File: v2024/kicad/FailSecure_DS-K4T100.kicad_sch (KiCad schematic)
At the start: 82 parts, among them CN1 WJ2EDGRC-5.08-2P, CN2 WJ2EDGRC-5.08-2P, CN3 WJ2EDGRC-5.08-8P, CN4 WAFER-200W-4P, CN5 WJ2EDGRC-5.08-2P, Q1 BSS138, Q3 BSS138, Q4 BSS138, SW1 1TS002B-2300-4301, SW2 1TS002B-2300-4301, U1 PicoW, U2 TPS563200DDCR, U3 BX-DS2.54-4PTP, U4 SFH6206-3T, U5 HX PM2.54-2X5P WT, U6 HX PM2.54-2X5P WT

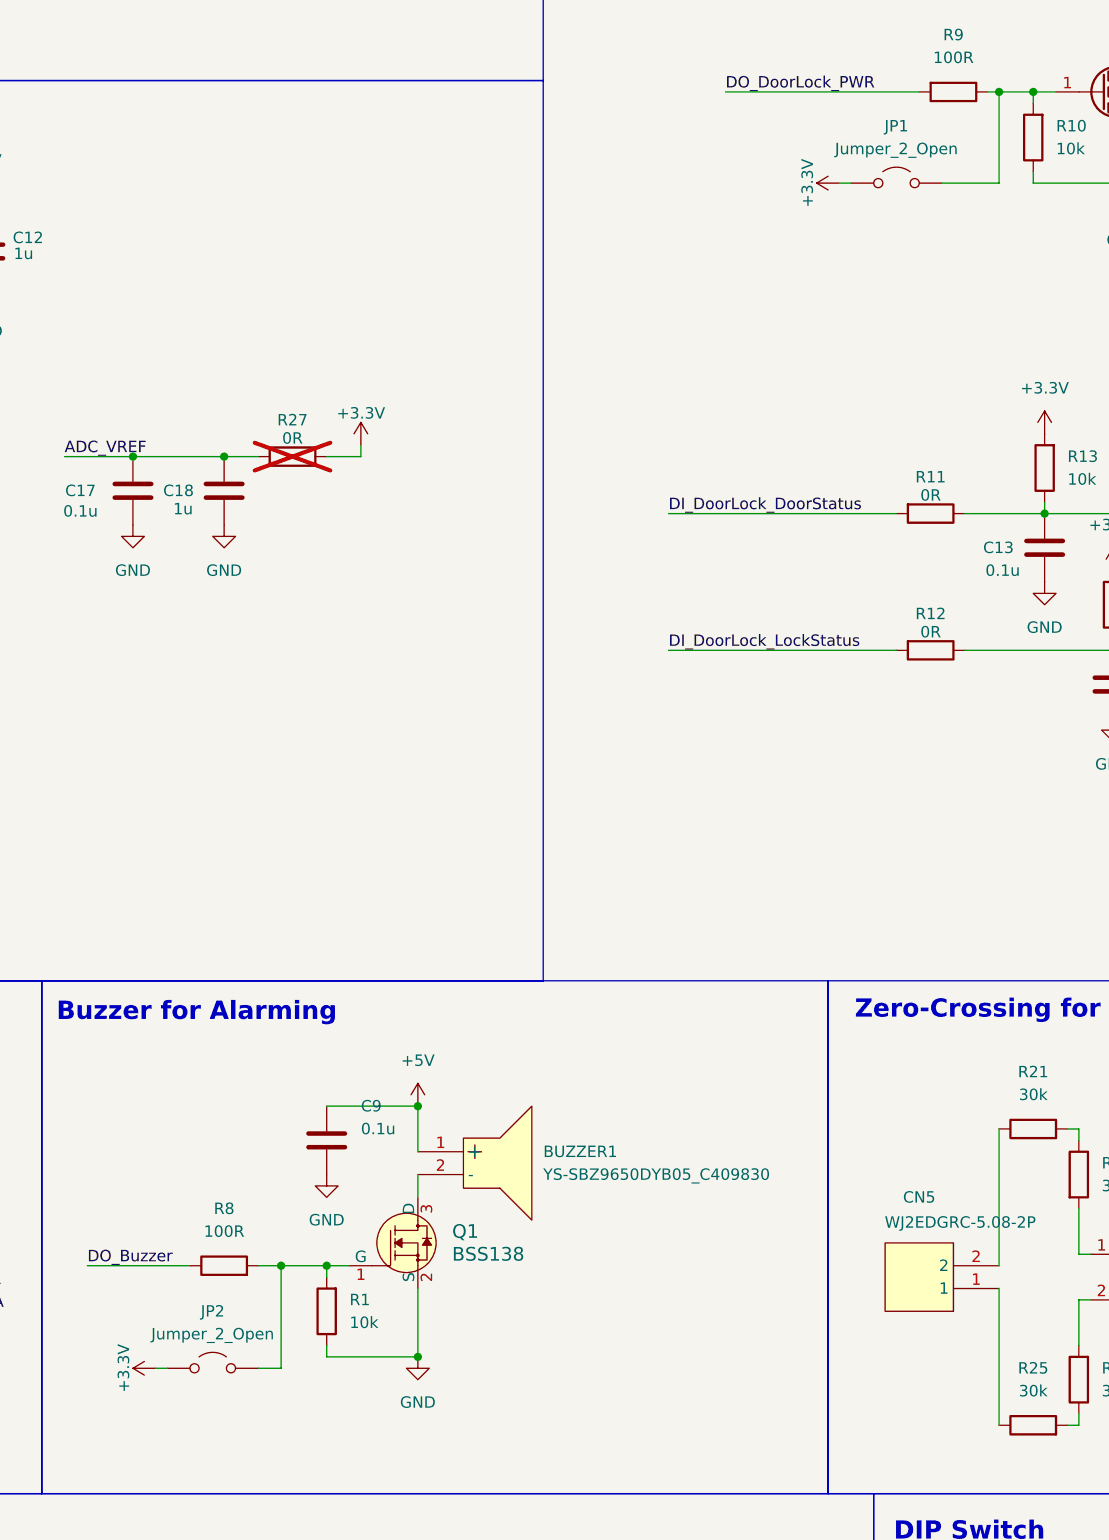
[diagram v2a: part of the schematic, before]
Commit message: Kicad, add LCSC part number to forgotten devices & Don't populate jumper
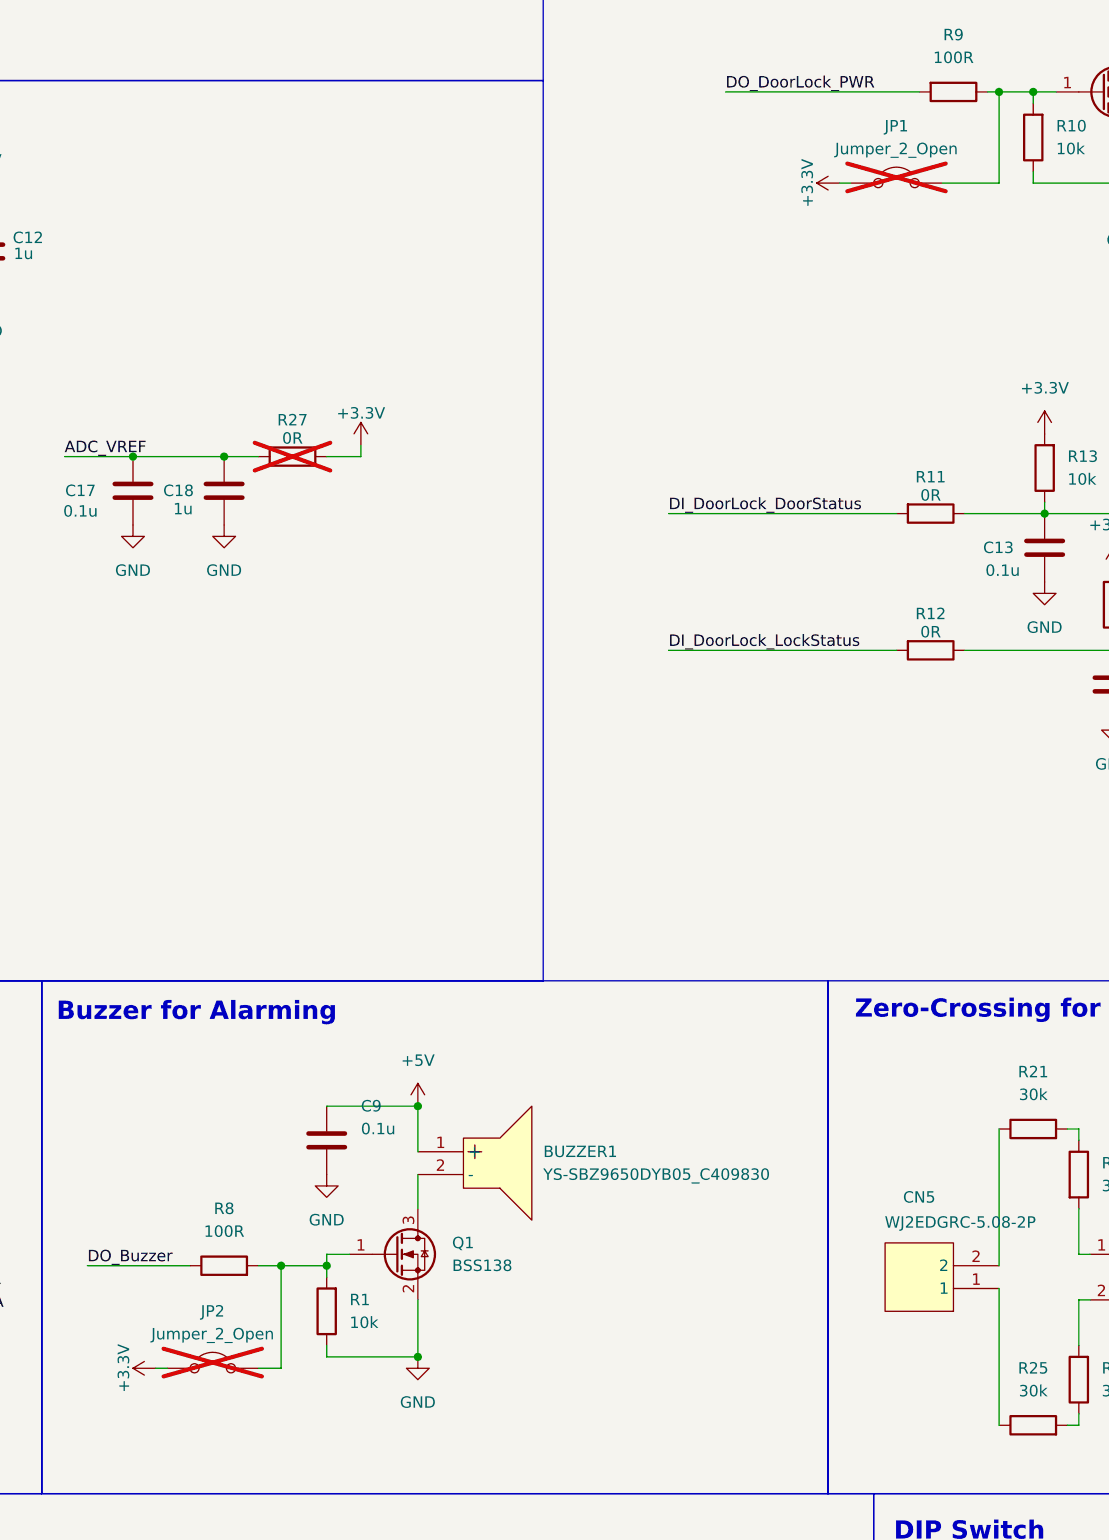
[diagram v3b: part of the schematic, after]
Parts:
- removed Q1: BSS138, digikey-footprints:SOT-23-3, symbol dk_Transistors-FETs-MOSFETs-Single:BSS138
- added Q1: BSS138, Package_TO_SOT_SMD:SOT-23-3, symbol Transistor_FET:BSS138
- D6, D7: LCSC Part (none) -> C148225
- JP1, JP2: now not fitted
- Q3, Q4: LCSC Part (none) -> C431507
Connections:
- net GND: now also Q1.2 (S)
- net at JP2.2 (B), R1.2, R8.2: now also Q1.1 (G)
- net at BUZZER1.2 (-): now also Q1.3 (D)
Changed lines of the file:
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@@
 	(wire
 		(pts
+			(xy 163.83 200.66) (xy 163.83 201.93)
+		)
+		(stroke
+			(width 0)
+			(type default)
+		)
+	)
+	(wire
+		(pts
 			(xy 107.95 107.95) (xy 92.71 107.95)
 		)
@@
 	(wire
 		(pts
-			(xy 173.99 194.31) (xy 173.99 191.77)
+			(xy 173.99 195.58) (xy 173.99 191.77)
 		)
 		(stroke
@@
 	(wire
 		(pts
-			(xy 163.83 201.93) (xy 166.37 201.93)
+			(xy 163.83 200.66) (xy 166.37 200.66)
 		)
 		(stroke
@@
 	(wire
 		(pts
-			(xy 173.99 204.47) (xy 173.99 212.09)
+			(xy 173.99 205.74) (xy 173.99 212.09)
 		)
 		(stroke
@@
 	)
 	(symbol
+		(lib_id "Transistor_FET:BSS138")
+		(at 171.45 200.66 0)
+		(unit 1)
+		(exclude_from_sim no)
+		(in_bom yes)
+		(on_board yes)
+		(dnp no)
+		(fields_autoplaced yes)
+		(property "Reference" "Q1"
+			(at 177.8 199.3899 0)
+			(effects
+				(font
+					(size 1.27 1.27)
+				)
+				(justify left)
+			)
+		)
+		(property "Value" "BSS138"
+			(at 177.8 201.9299 0)
+			(effects
+				(font
+					(size 1.27 1.27)
+				)
+				(justify left)
+			)
+		)
+		(property "Footprint" "Package_TO_SOT_SMD:SOT-23-3"
+			(at 176.53 202.565 0)
+			(effects
+				(font
+					(size 1.27 1.27)
+					(italic yes)
+				)
+				(justify left)
+				(hide yes)
+			)
+		)
+		(property "Datasheet" "https://www.onsemi.com/pub/Collateral/BSS138-D.PDF"
+			(at 176.53 204.47 0)
+			(effects
+				(font
+					(size 1.27 1.27)
+				)
+				(justify left)
+				(hide yes)
+			)
+		)
+		(property "Description" "50V Vds, 0.22A Id, N-Channel MOSFET, SOT-23"
+			(at 171.45 200.66 0)
+			(effects
+				(font
+					(size 1.27 1.27)
+				)
+				(hide yes)
+			)
+		)
+		(property "LCSC Part" "C431507"
+			(at 171.45 200.66 0)
+			(effects
+				(font
+					(size 1.27 1.27)
+				)
+				(hide yes)
+			)
+		)
+		(pin "3"
+		)
+		(pin "2"
+		)
+		(pin "1"
+		)
+		(instances
+			(project "FailSecure_DS-K4T100"
+				(path "/4175a3da-4c52-428e-a864-babd20cead6f"
+					(reference "Q1")
+					(unit 1)
+				)
+			)
+		)
+	)
+	(symbol
 		(lib_id "power:GND")
 		(at 114.3 92.71 0)
@@
 		(in_bom yes)
 		(on_board yes)
-		(dnp no)
+		(dnp yes)
 		(fields_autoplaced yes)
 		(property "Reference" "JP1"
@@
 			)
 		)
+		(property "LCSC Part" "C148225"
+			(at 368.3 58.42 90)
+			(effects
+				(font
+					(size 1.27 1.27)
+				)
+				(hide yes)
+			)
+		)
 		(pin "2"
 		)
@@
 			)
 		)
+		(property "LCSC Part" "C431507"
+			(at 350.52 60.96 0)
+			(effects
+				(font
+					(size 1.27 1.27)
+				)
+				(hide yes)
+			)
+		)
 		(pin "3"
 		)
@@
 			)
 		)
+		(property "LCSC Part" "C431507"
+			(at 250.19 71.12 0)
+			(effects
+				(font
+					(size 1.27 1.27)
+				)
+				(hide yes)
+			)
+		)
 		(pin "3"
 		)
@@
 		(in_bom yes)
 		(on_board yes)
-		(dnp no)
+		(dnp yes)
 		(fields_autoplaced yes)
 		(property "Reference" "JP2"
@@
 	)
 	(symbol
-		(lib_id "dk_Transistors-FETs-MOSFETs-Single:BSS138")
-		(at 173.99 199.39 0)
-		(unit 1)
-		(exclude_from_sim no)
-		(in_bom yes)
-		(on_board yes)
-		(dnp no)
-		(fields_autoplaced yes)
-		(property "Reference" "Q1"
-			(at 177.8 198.1199 0)
-			(effects
-				(font
-					(size 1.524 1.524)
-				)
-				(justify left)
-			)
-		)
-		(property "Value" "BSS138"
-			(at 177.8 200.6599 0)
-			(effects
-				(font
-					(size 1.524 1.524)
-				)
-				(justify left)
-			)
-		)
-		(property "Footprint" "digikey-footprints:SOT-23-3"
-			(at 179.07 194.31 0)
-			(effects
-				(font
-					(size 1.524 1.524)
-				)
-				(justify left)
-				(hide yes)
-			)
-		)
-		(property "Datasheet" "https://www.onsemi.com/pub/Collateral/BSS138-D.PDF"
-			(at 179.07 191.77 0)
-			(effects
-				(font
-					(size 1.524 1.524)
-				)
-				(justify left)
-				(hide yes)
-			)
-		)
-		(property "Description" "MOSFET N-CH 50V 220MA SOT-23"
-			(at 173.99 199.39 0)
-			(effects
-				(font
-					(size 1.27 1.27)
-				)
-				(hide yes)
-			)
-		)
-		(property "Digi-Key_PN" "BSS138CT-ND"
-			(at 179.07 189.23 0)
-			(effects
-				(font
-					(size 1.524 1.524)
-				)
-				(justify left)
-				(hide yes)
-			)
-		)
-		(property "MPN" "BSS138"
-			(at 179.07 186.69 0)
-			(effects
-				(font
-					(size 1.524 1.524)
-				)
-				(justify left)
-				(hide yes)
-			)
-		)
-		(property "Category" "Discrete Semiconductor Products"
-			(at 179.07 184.15 0)
-			(effects
-				(font
-					(size 1.524 1.524)
-				)
-				(justify left)
-				(hide yes)
-			)
-		)
-		(property "Family" "Transistors - FETs, MOSFETs - Single"
-			(at 179.07 181.61 0)
-			(effects
-				(font
-					(size 1.524 1.524)
-				)
-				(justify left)
-				(hide yes)
-			)
-		)
-		(property "DK_Datasheet_Link" "https://www.onsemi.com/pub/Collateral/BSS138-D.PDF"
-			(at 179.07 179.07 0)
-			(effects
-				(font
-					(size 1.524 1.524)
-				)
-				(justify left)
-				(hide yes)
-			)
-		)
-		(property "DK_Detail_Page" "/product-detail/en/on-semiconductor/BSS138/BSS138CT-ND/244294"
-			(at 179.07 176.53 0)
-			(effects
-				(font
-					(size 1.524 1.524)
-				)
-				(justify left)
-				(hide yes)
-			)
-		)
-		(property "Description_1" "MOSFET N-CH 50V 220MA SOT-23"
-			(at 179.07 173.99 0)
-			(effects
-				(font
-					(size 1.524 1.524)
-				)
-				(justify left)
-				(hide yes)
-			)
-		)
-		(property "Manufacturer" "ON Semiconductor"
-			(at 179.07 171.45 0)
-			(effects
-				(font
-					(size 1.524 1.524)
-				)
-				(justify left)
-				(hide yes)
-			)
-		)
-		(property "Status" "Active"
-			(at 179.07 168.91 0)
-			(effects
-				(font
-					(size 1.524 1.524)
-				)
-				(justify left)
-				(hide yes)
-			)
-		)
-		(property "LCSC Part" "C431507"
-			(at 173.99 199.39 0)
-			(effects
-				(font
-					(size 1.27 1.27)
-				)
-				(hide yes)
-			)
-		)
-		(pin "3"
-		)
-		(pin "2"
-		)
-		(pin "1"
-		)
-		(instances
-			(project "FailSecure_DS-K4T100"
-				(path "/4175a3da-4c52-428e-a864-babd20cead6f"
-					(reference "Q1")
-					(unit 1)
-				)
-			)
-		)
-	)
-	(symbol
 		(lib_id "power:GND")
 		(at 265.43 210.82 0)
@@
 			(effects
 				(font
+					(size 1.27 1.27)
+				)
+				(hide yes)
+			)
+		)
+		(property "LCSC Part" "C148225"
+			(at 232.41 49.53 90)
+			(effects
+				(font

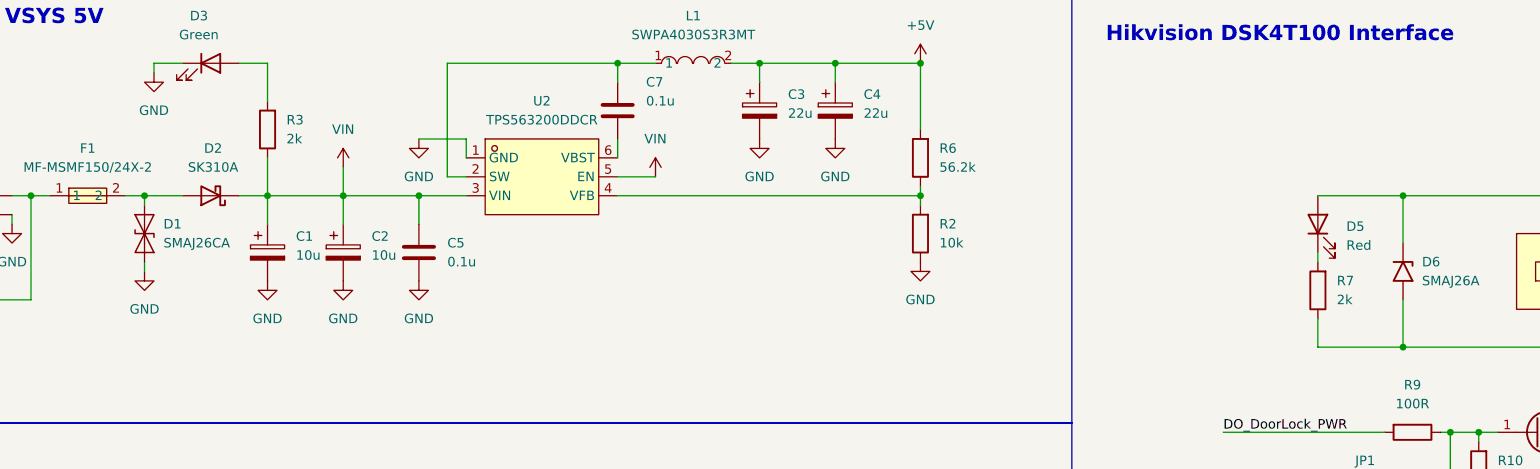
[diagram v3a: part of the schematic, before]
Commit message: Update BOM by remove extended part as much as posible
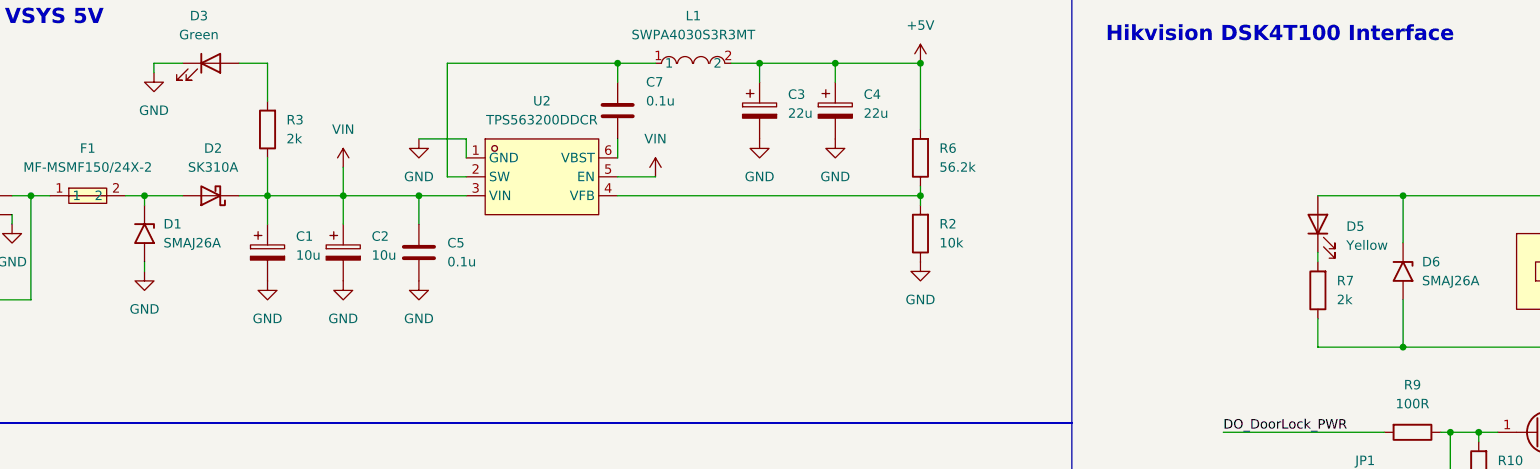
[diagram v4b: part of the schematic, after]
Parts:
- removed D1: SMAJ26CA, Diode_SMD:D_SMA, symbol Diode:SMAJ26CA
- added D1: SMAJ26A, Diode_SMD:D_SMA, symbol Diode:SMAJ26A
- D5: value Red -> Yellow; LCSC Part C2295 -> C2296
- R11, R12, R23, R31: LCSC Part C304185 -> C21189
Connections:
- net GND: now also D1.2 (A2)
- net at D2.2 (A), F1.2: now also D1.1 (A1)
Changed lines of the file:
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@@
 			)
 		)
-		(property "Value" "Red"
+		(property "Value" "Yellow"
 			(at 224.79 46.0374 90)
 			(effects
@@
 			)
 		)
-		(property "LCSC Part" "C2295"
+		(property "LCSC Part" "C2296"
 			(at 220.98 43.18 90)
 			(effects
@@
 			)
 		)
-		(property "LCSC Part" "C304185"
+		(property "LCSC Part" "C21189"
 			(at 231.14 118.11 90)
 			(effects
@@
 			)
 		)
-		(property "LCSC Part" "C304185"
+		(property "LCSC Part" "C21189"
 			(at 279.4 199.39 90)
 			(effects
@@
 	)
 	(symbol
-		(lib_id "Diode:SMAJ26CA")
-		(at 63.5 44.45 90)
-		(unit 1)
-		(exclude_from_sim no)
-		(in_bom yes)
-		(on_board yes)
-		(dnp no)
-		(fields_autoplaced yes)
-		(property "Reference" "D1"
-			(at 66.04 43.1799 90)
-			(effects
-				(font
-					(size 1.27 1.27)
-				)
-				(justify right)
-			)
-		)
-		(property "Value" "SMAJ26CA"
-			(at 66.04 45.7199 90)
-			(effects
-				(font
-					(size 1.27 1.27)
-				)
-				(justify right)
-			)
-		)
-		(property "Footprint" "Diode_SMD:D_SMA"
-			(at 68.58 44.45 0)
-			(effects
-				(font
-					(size 1.27 1.27)
-				)
-				(hide yes)
-			)
-		)
-		(property "Datasheet" "https://www.littelfuse.com/media?resourcetype=datasheets&itemid=75e32973-b177-4ee3-a0ff-cedaf1abdb93&filename=smaj-datasheet"
-			(at 63.5 44.45 0)
-			(effects
-				(font
-					(size 1.27 1.27)
-				)
-				(hide yes)
-			)
-		)
-		(property "Description" "400W bidirectional Transient Voltage Suppressor, 26.0Vr, SMA(DO-214AC)"
-			(at 63.5 44.45 0)
-			(effects
-				(font
-					(size 1.27 1.27)
-				)
-				(hide yes)
-			)
-		)
-		(property "LCSC Part" "C173517"
-			(at 63.5 44.45 90)
-			(effects
-				(font
-					(size 1.27 1.27)
-				)
-				(hide yes)
-			)
-		)
-		(pin "1"
-		)
-		(pin "2"
-		)
-		(instances
-			(project ""
-				(path "/4175a3da-4c52-428e-a864-babd20cead6f"
-					(reference "D1")
-					(unit 1)
-				)
-			)
-		)
-	)
-	(symbol
 		(lib_id "YS-SBZ9650DYB05:YS-SBZ9650DYB05_C409830")
 		(at 179.07 189.23 180)
@@
 	)
 	(symbol
+		(lib_id "Diode:SMAJ26A")
+		(at 63.5 44.45 270)
+		(unit 1)
+		(exclude_from_sim no)
+		(in_bom yes)
+		(on_board yes)
+		(dnp no)
+		(fields_autoplaced yes)
+		(property "Reference" "D1"
+			(at 66.04 43.1799 90)
+			(effects
+				(font
+					(size 1.27 1.27)
+				)
+				(justify left)
+			)
+		)
+		(property "Value" "SMAJ26A"
+			(at 66.04 45.7199 90)
+			(effects
+				(font
+					(size 1.27 1.27)
+				)
+				(justify left)
+			)
+		)
+		(property "Footprint" "Diode_SMD:D_SMA"
+			(at 58.42 44.45 0)
+			(effects
+				(font
+					(size 1.27 1.27)
+				)
+				(hide yes)
+			)
+		)
+		(property "Datasheet" "https://www.littelfuse.com/media?resourcetype=datasheets&itemid=75e32973-b177-4ee3-a0ff-cedaf1abdb93&filename=smaj-datasheet"
+			(at 63.5 43.18 0)
+			(effects
+				(font
+					(size 1.27 1.27)
+				)
+				(hide yes)
+			)
+		)
+		(property "Description" "400W unidirectional Transient Voltage Suppressor, 26.0Vr, SMA(DO-214AC)"
+			(at 63.5 44.45 0)
+			(effects
+				(font
+					(size 1.27 1.27)
+				)
+				(hide yes)
+			)
+		)
+		(property "LCSC Part" "C148225"
+			(at 63.5 44.45 90)
+			(effects
+				(font
+					(size 1.27 1.27)
+				)
+				(hide yes)
+			)
+		)
+		(pin "2"
+		)
+		(pin "1"
+		)
+		(instances
+			(project "FailSecure_DS-K4T100"
+				(path "/4175a3da-4c52-428e-a864-babd20cead6f"
+					(reference "D1")
+					(unit 1)
+				)
+			)
+		)
+	)
+	(symbol
 		(lib_id "power:GND")
 		(at 63.5 49.53 0)
@@
 			)
 		)
-		(property "LCSC Part" "C304185"
+		(property "LCSC Part" "C21189"
 			(at 165.1 255.27 90)
 			(effects
@@
 			)
 		)
-		(property "LCSC Part" "C304185"
+		(property "LCSC Part" "C21189"
 			(at 231.14 133.35 90)
 			(effects
